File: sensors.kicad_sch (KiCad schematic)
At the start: 0 parts

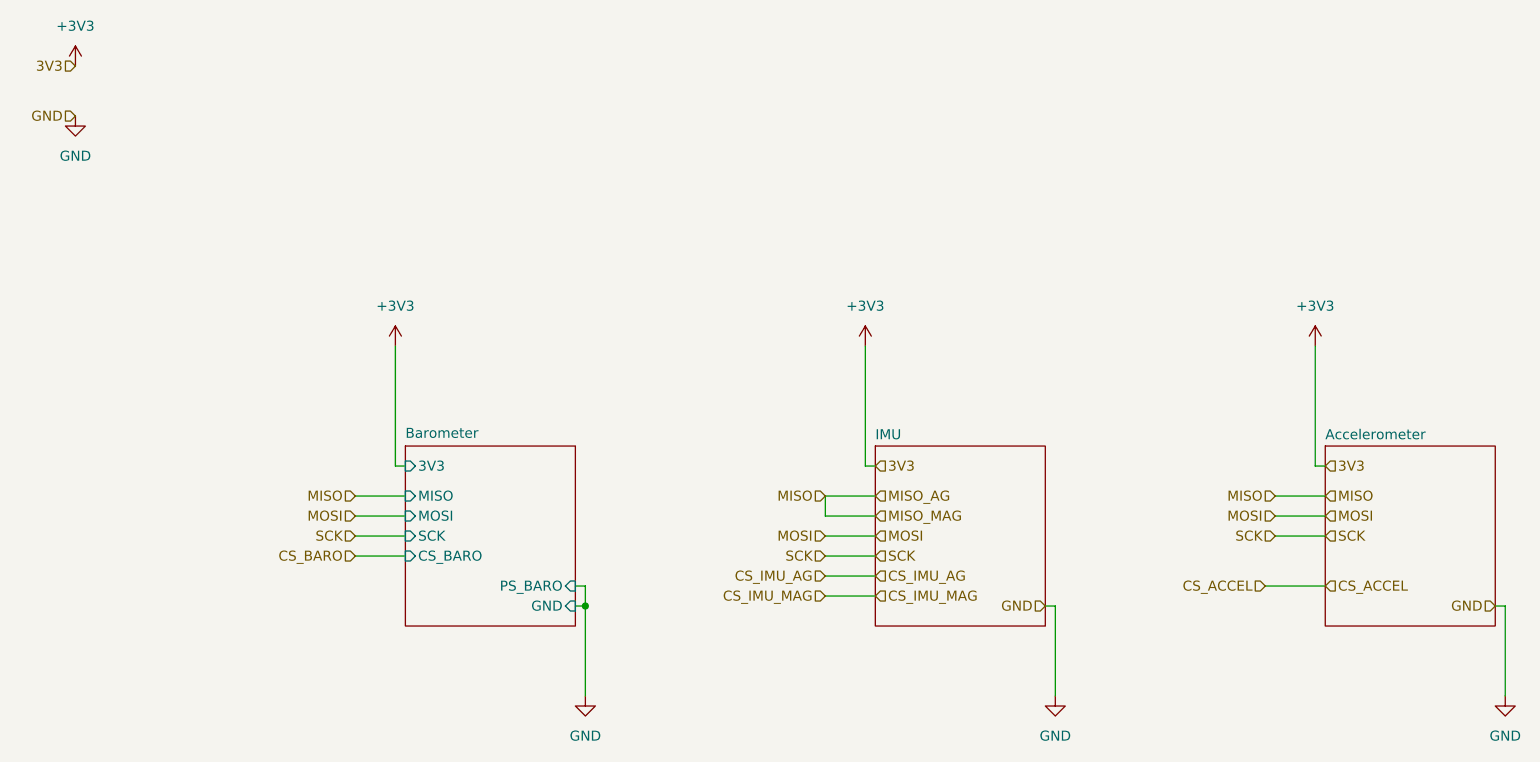
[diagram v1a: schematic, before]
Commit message: Connected topsheet
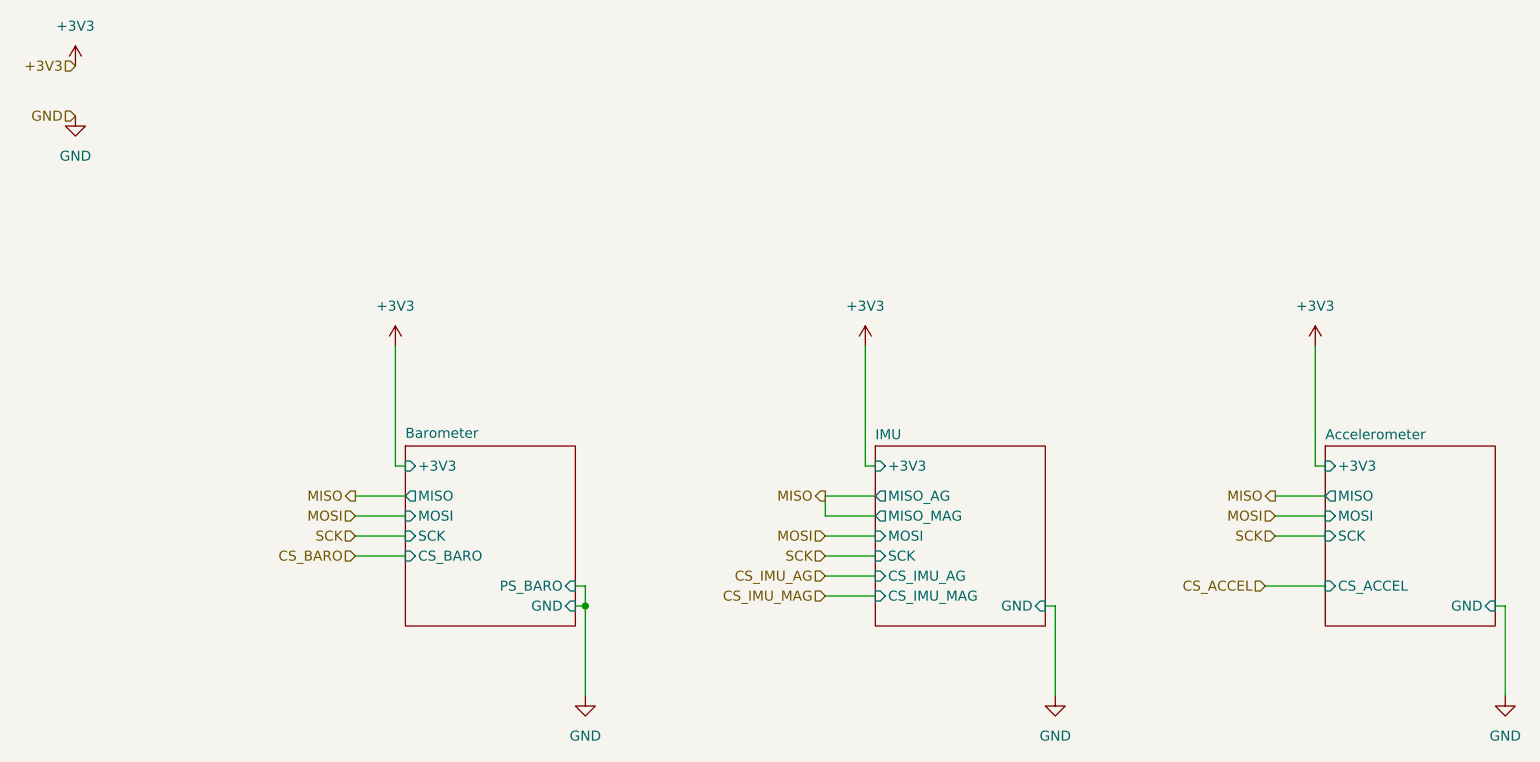
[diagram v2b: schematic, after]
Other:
- sheet Accelerometer ports: added +3V3, CS_ACCEL, GND, MISO, MOSI, SCK; removed none
- sheet Barometer ports: added +3V3; removed 3V3
- sheet IMU ports: added +3V3, CS_IMU_AG, CS_IMU_MAG, GND, MISO_AG, MISO_MAG, MOSI, SCK; removed none
